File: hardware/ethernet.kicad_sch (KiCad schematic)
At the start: 36 parts, among them J601 J0011D21BNL, U601 W5500, Y601 ECS-250-18-5PX-F-TR

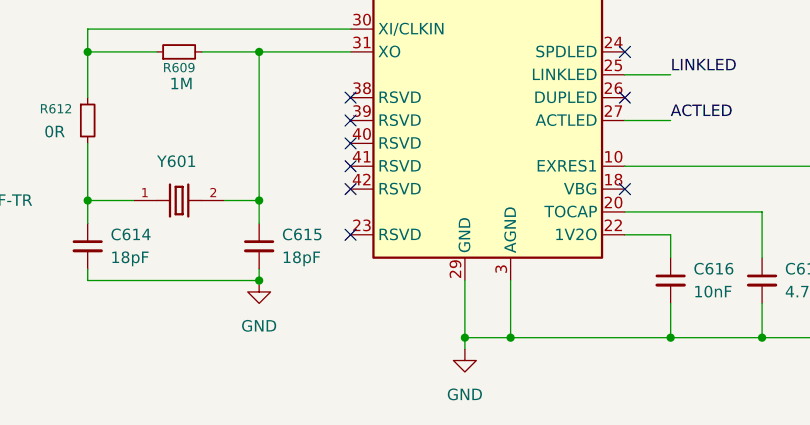
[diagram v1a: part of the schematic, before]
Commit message: ethernet/wisun pcb update
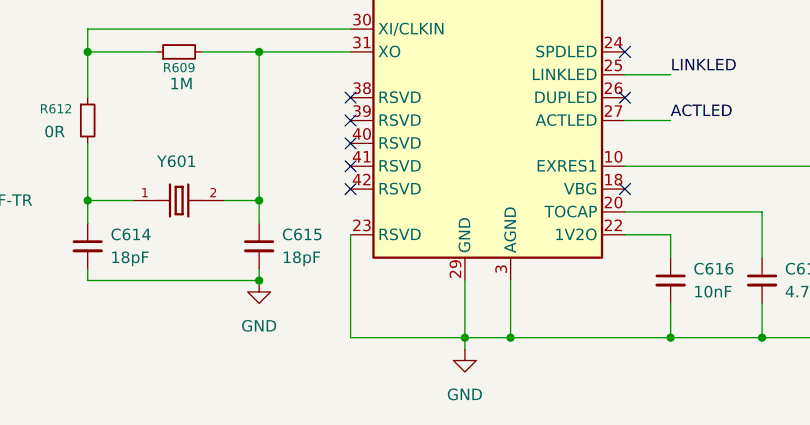
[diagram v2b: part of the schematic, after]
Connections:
- net GND: now also U601.23 (RSVD)
- no-connect marks 10 -> 9
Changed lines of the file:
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@@
-	)
-	(no_connect
-		(at 86.36 135.89)
 	)
 	(no_connect
@@
 	(wire
 		(pts
+			(xy 86.36 135.89) (xy 86.36 147.32)
+		)
+		(stroke
+			(width 0)
+			(type default)
+		)
+	)
+	(wire
+		(pts
 			(xy 195.58 144.78) (xy 212.09 144.78)
 		)
@@
 		)
 		(stroke
+			(width 0)
+			(type default)
+		)
+	)
+	(wire
+		(pts
+			(xy 86.36 147.32) (xy 99.06 147.32)
+		)
+		(stroke

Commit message: Power Layout WIP
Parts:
- removed C611: 1nF/2kV, Capacitor_SMD:C_0805_2012Metric, symbol Device:C_Small
- renumbered C612 to C611, C613 to C612, C614 to C613, C615 to C614, C616 to C615, C617 to C616, R602 to R601, R603 to R602, R604 to R603, R605 to R604, R606 to R605, R607 to R606, R608 to R607, R601 to R608
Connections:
- net +3.3VA: now also FB601.2; no longer R608.1
- net GND: now also R608.2
- net at J601.8: now also R608.1
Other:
- moved on the sheet: FB601, R608

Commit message: ethernet cap layout
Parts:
- C601, C602, C603, C604, C605, C606, C607, C608: footprint Capacitor_SMD:C_0805_2012Metric -> Capacitor_SMD:C_0603_1608Metric
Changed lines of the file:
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@@
 			)
 		)
-		(property "Footprint" "Capacitor_SMD:C_0805_2012Metric"
+		(property "Footprint" "Capacitor_SMD:C_0603_1608Metric"
 			(at 73.66 53.34 0)
 			(effects
@@
 			)
 		)
-		(property "Footprint" "Capacitor_SMD:C_0805_2012Metric"
+		(property "Footprint" "Capacitor_SMD:C_0603_1608Metric"
 			(at 161.29 53.34 0)
 			(effects
@@
 			)
 		)
-		(property "Footprint" "Capacitor_SMD:C_0805_2012Metric"
+		(property "Footprint" "Capacitor_SMD:C_0603_1608Metric"
 			(at 151.13 53.34 0)
 			(effects
@@
 			)
 		)
-		(property "Footprint" "Capacitor_SMD:C_0805_2012Metric"
+		(property "Footprint" "Capacitor_SMD:C_0603_1608Metric"
 			(at 140.97 53.34 0)
 			(effects
@@
 			)
 		)
-		(property "Footprint" "Capacitor_SMD:C_0805_2012Metric"
+		(property "Footprint" "Capacitor_SMD:C_0603_1608Metric"
 			(at 130.81 53.34 0)
 			(effects
@@
 			)
 		)
-		(property "Footprint" "Capacitor_SMD:C_0805_2012Metric"
+		(property "Footprint" "Capacitor_SMD:C_0603_1608Metric"
 			(at 110.49 53.34 0)
 			(effects
@@
 			)
 		)
-		(property "Footprint" "Capacitor_SMD:C_0805_2012Metric"
+		(property "Footprint" "Capacitor_SMD:C_0603_1608Metric"
 			(at 120.65 53.34 0)
 			(effects
@@
 			)
 		)
-		(property "Footprint" "Capacitor_SMD:C_0805_2012Metric"
+		(property "Footprint" "Capacitor_SMD:C_0603_1608Metric"
 			(at 83.82 53.34 0)
 			(effects

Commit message: PCB Layout - Rev 1.0
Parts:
- added R606: 10K, Resistor_SMD:R_0603_1608Metric, symbol Device:R_Small
- renumbered R606 to R607, R607 to R608, R608 to R609, R609 to R610, R610 to R611, R611 to R612, R612 to R613, R613 to R614, R614 to R615, R615 to R616
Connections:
- net +3.3V: now also R606.2
- net W5500_RST: now also R606.1

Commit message: label cleanup
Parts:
- R609: value 0 -> 0R
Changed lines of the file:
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@@
 			)
 		)
-		(property "Value" "0"
+		(property "Value" "0R"
 			(at 196.85 110.4899 0)
 			(effects

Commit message: values subbed
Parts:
- R609, R613: value 0R -> 0.05R
- R611, R612: value 49.9R -> 51R
- R615: value 12.4K -> 12K
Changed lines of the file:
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@@
 			)
 		)
-		(property "Value" "49.9R"
+		(property "Value" "51R"
 			(at 160.274 116.84 0)
 			(effects
@@
 			)
 		)
-		(property "Value" "12.4K"
+		(property "Value" "12K"
 			(at 144.78 141.986 0)
 			(effects
@@
 			)
 		)
-		(property "Value" "0R"
+		(property "Value" "0.05R"
 			(at 196.85 110.4899 0)
 			(effects
@@
 			)
 		)
-		(property "Value" "49.9R"
+		(property "Value" "51R"
 			(at 151.384 116.84 0)
 			(effects
@@
 			)
 		)
-		(property "Value" "0R"
-			(at 52.324 124.46 0)
-			(effects
-				(font
+		(property "Value" "0.05R"
+			(at 50.038 124.206 0)
+			(effects
+				(font
